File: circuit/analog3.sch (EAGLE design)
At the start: 71 parts, among them IC1 AD8603UJ, IC2 74HC4052D, IC3 AD8603UJ, IC4 AD8221R, IC5 AD8221R, IC6 LM258, IC7 LM258

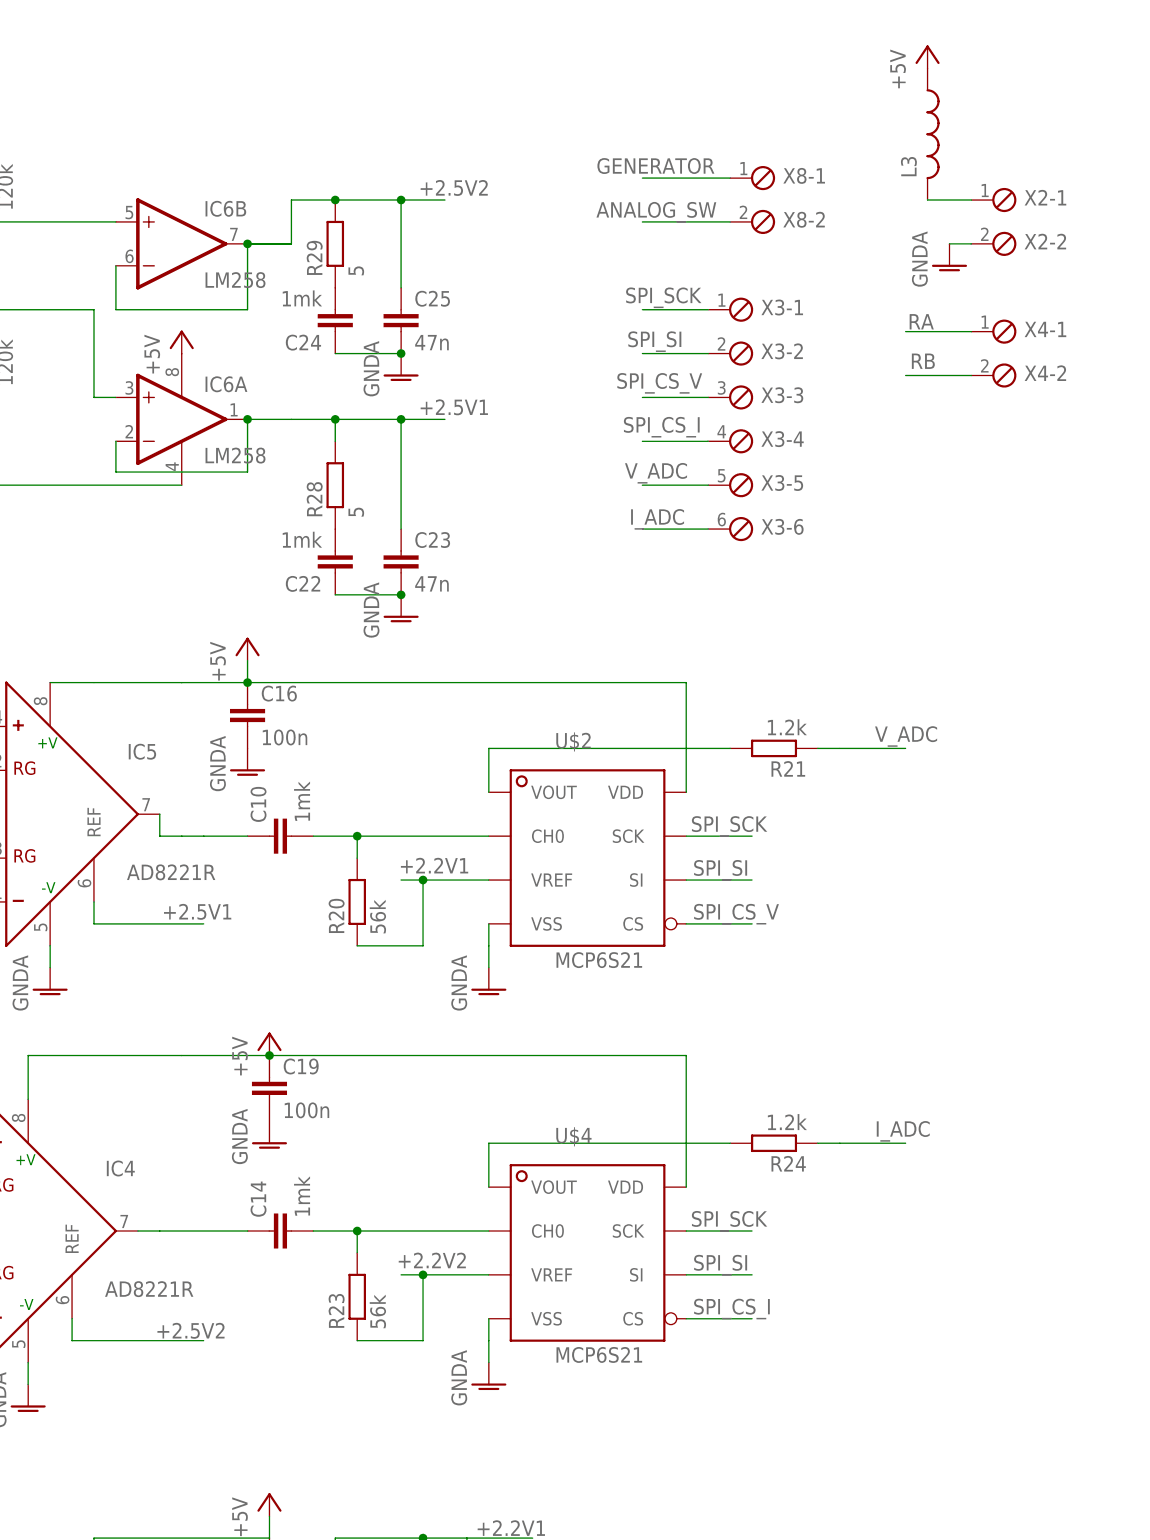
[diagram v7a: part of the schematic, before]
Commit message: - совместили северные контакты - добавили RC цепочки между первым и вторым каскадом усиления - добавили неподключеный коннектор, чтобы было на чем держаться дисплею
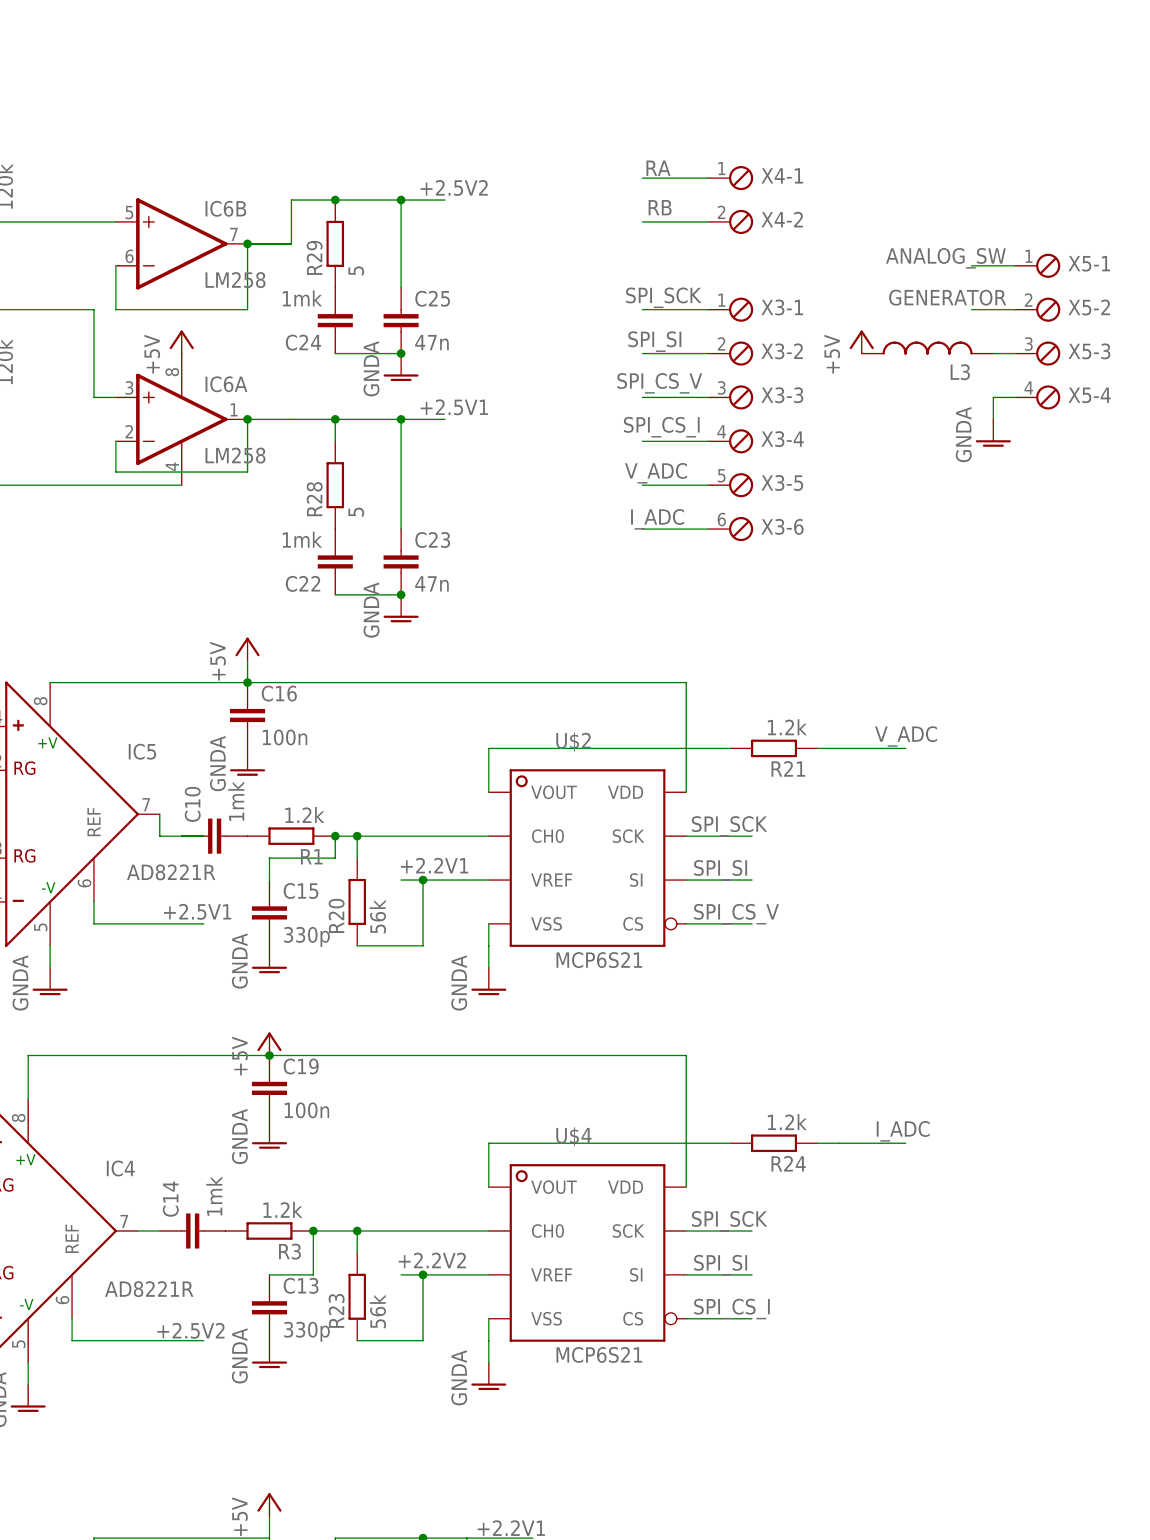
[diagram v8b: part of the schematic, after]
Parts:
- removed X2, X8: (no value), con-phoenix-254:MPT2
- added C13, C15: 330p, rcl:C-EUC0805
- added R1, R3: 1.2k, rcl:R-EU_R0603
- added X5: (no value), con-phoenix-254:MPT4
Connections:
- new net N$37: C10.2, R1.2
- new net N$38: C14.2, R3.2
- net ANALOG_SW: now also X5-1.1; no longer X8-2.1
- net GENERATOR: now also X5-2.1; no longer X8-1.1
- net GNDA: now also C13.2, C15.2, X5-4.1; no longer X2-2.1
- net N$25: now also C13.1, R3.1; no longer C14.2
- net N$27: now also C15.1, R1.1; no longer C10.2
- net N$6: now also X5-3.1; no longer X2-1.1
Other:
- moved on the sheet: C10, C14, L3, X4-1, X4-2
